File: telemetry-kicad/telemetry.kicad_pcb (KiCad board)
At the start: 4 copper layers, 94 x 83.5 mm, 97 parts, among them J1 2601-1102, J2 RFPC-SMA27-F, J3 TC2030, J4 2601-1102, J5 2601-1102, J6 USB_C_Receptacle_USB2.0_16P, J7 SD_Card_Receptacle, Q1 DMP3099LQ-7, SW1 SW_NRST, SW2 SW_BOOT0, U1 LMR33610ADDAR, U10 TLC59108IPWR, U11 MCP1703T-5002E/CB, U2 ASM330LHHXG1TR, U3 MAX-M10S-00B, U4 TCAN337, U5 STM32H523RCT7, U6 TCAN337, U7 USBLC6-2SC6, U9 TLC59108IPWR, Y1 ABM8AIG-24.000MHz-8-2Z-T

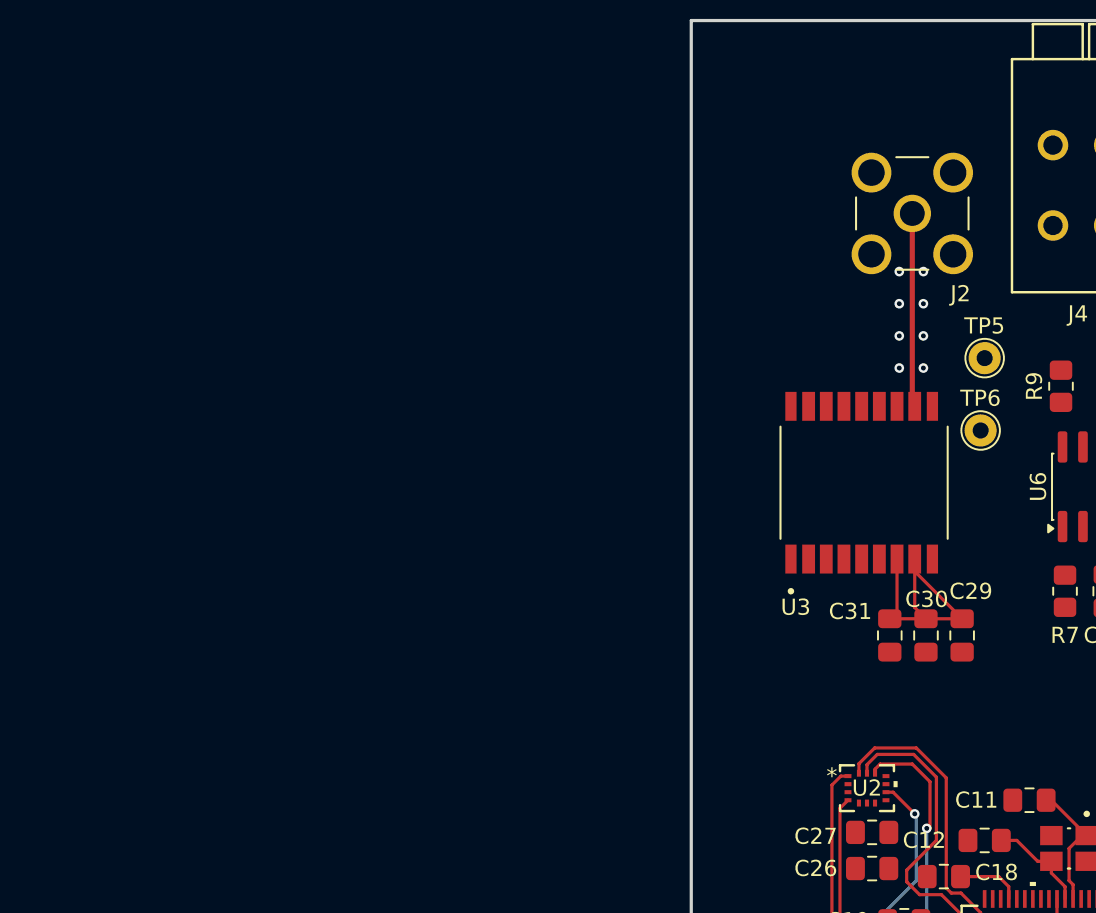
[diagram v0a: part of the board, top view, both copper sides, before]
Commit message: Changed ublox MAX-M10 to Quectel LC29HBAMD to enable the option of using RTK as well as keeping the dead reckoning features
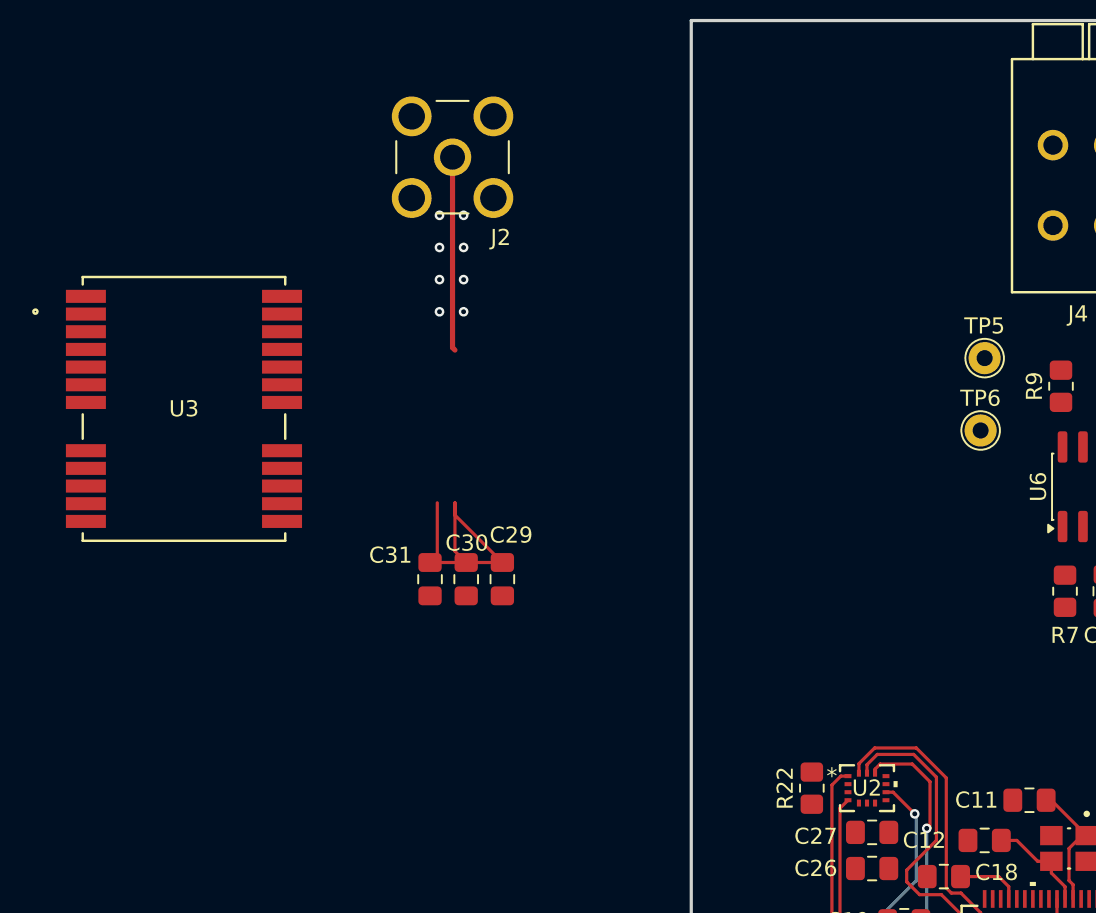
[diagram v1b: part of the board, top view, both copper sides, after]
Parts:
- added R22: 10K, Resistor_SMD:R_0805_2012Metric_Pad1.20x1.40mm_HandSolder, F.Cu at (19.5, 59.8)
- U3: value MAX-M10S-00B -> LC29HIAMD; footprint telemetry:MAX-M10S-00B -> telemetry:LC29HAAMD
- moved U3 42.4 mm to (-19.6, 36.2), turned to 0 degrees
- moved C29 28.8 mm to (0.25, 46.8)
- moved C30 28.8 mm to (-2.00, 46.8)
- moved C31 28.8 mm to (-4.25, 46.8)
- moved J2 28.8 mm to (-2.85, 20.5)
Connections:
- C32 pad 2: V_IN -> VBUS_USB
- C33 pad 2: +5V -> +3.3V
- C34 pad 2: +5V -> +3.3V
- D6 pad 1: V_IN -> VBUS_USB
- U10 pad 20: +5V -> +3.3V
- U11 pad 3: V_IN -> VBUS_USB
- U3 pad 1: GND -> unconnected-(U3-BOOT-Pad1)
- U3 pad 11: ANT -> unconnected-(U3-RF_IN-Pad11)
- U3 pad 13: unconnected-(U3-LNA_EN-Pad13) -> GND
- U3 pad 2: TXD_GNSS -> unconnected-(U3-FWD-Pad2)
- U3 pad 3: RXD_GNSS -> unconnected-(U3-1PPS-Pad3)
- U3 pad 4: TIMEPULSE_GNSS -> unconnected-(U3-WHEELTICK-Pad4)
- U3 pad 7: +3.3V -> unconnected-(U3-RESERVED-Pad7)
- U3 pad 8: +3.3V -> unconnected-(U3-RESET_N-Pad8)
- U5 pad 33: TXD_CAN2 -> RXD_CAN2
- U5 pad 34: RXD_CAN2 -> TXD_CAN2
- U9 pad 20: +5V -> +3.3V
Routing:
- net +5V: track 4.75 -> 0.00 mm
- net +3.3V: track 66.0 -> 70.7 mm

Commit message: small fixes
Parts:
- added C28: 100nF, Capacitor_SMD:C_0805_2012Metric_Pad1.18x1.45mm_HandSolder, F.Cu at (-27.7, 78.8)
- added C36: 100nF, Capacitor_SMD:C_0805_2012Metric_Pad1.18x1.45mm_HandSolder, F.Cu at (-27.7, 81.8)
- added C37: 10uF, Capacitor_SMD:C_0805_2012Metric_Pad1.18x1.45mm_HandSolder, F.Cu at (-27.7, 84.8)
- added C38: 100nF, Capacitor_SMD:C_0805_2012Metric_Pad1.18x1.45mm_HandSolder, F.Cu at (-27.7, 87.8)
- added C39: 1uF, Capacitor_SMD:C_0805_2012Metric_Pad1.18x1.45mm_HandSolder, F.Cu at (-27.7, 90.9)
- added R24: 10k, Resistor_SMD:R_0805_2012Metric_Pad1.20x1.40mm_HandSolder, F.Cu at (-14.6, 86.8)
- added R25: R_US, Resistor_THT:R_Array_SIP4, F.Cu at (-39.9, 61.6)
- added R26: R_US, Resistor_THT:R_Array_SIP4, F.Cu at (-39.9, 65.8)
- added R29: R_US, Resistor_THT:R_Array_SIP4, F.Cu at (-39.9, 69.9)
- added R30: R_US, Resistor_THT:R_Array_SIP4, F.Cu at (-39.9, 74.1)
- added R31: 21.5k, Resistor_THT:R_Array_SIP4, F.Cu at (-39.9, 78.3)
- added U13: TXS0108EPW, Package_SO:TSSOP-20_4.4x6.5mm_P0.65mm, F.Cu at (-20.6, 81.3)
- added U8: TPS2121RUXR, telemetry:VQFN-HR-12_L2.5-W2.0-P0.50-BL, F.Cu at (-15.0, 90.0)
- R27: value 1.1k -> 1.87k
- R28: value 3.74k -> 8.66k
- U3: value LC29HIAMD -> LC29HBAMD; footprint telemetry:LC29HAAMD -> telemetry:LC29HBAMD
- moved D6 100.8 mm to (-21.1, 88.1), turned to 0 degrees
- moved U3 32.3 mm to (-20.2, 68.4)
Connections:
- C2 pad 1: VBUS_USB -> V_HV
- C3 pad 1: VBUS_USB -> V_HV
- C32 pad 2: VBUS_USB -> V_HV
- D1 pad 1: VBUS_USB -> V_HV
- D6 pad 1: VBUS_USB -> +12V
- J1 pad 1: V_IN -> +12V
- J1 pad 2: V_IN -> +12V
- Q1 pad 2: VBUS_USB -> V_HV
- TP1 pad 1: VBUS_USB -> V_HV
- U1 pad 2: VBUS_USB -> V_HV
- U1 pad 3: VBUS_USB -> V_HV
- U11 pad 3: VBUS_USB -> V_HV
- U3 pad 11: unconnected-(U3-RF_IN-Pad11) -> ANT
- U3 pad 18: unconnected-(U3-CTS/SPI_MOSI-Pad18) -> CS_GNSS_1.8V
- U3 pad 19: unconnected-(U3-RTS/SPI_MISO-Pad19) -> CLK_GNSS_1.8V
- U3 pad 20: unconnected-(U3-TXD/SPI_CLK-Pad20) -> MISO_GNSS_1.8V
- U3 pad 21: unconnected-(U3-RXD/SPI_CS-Pad21) -> MOSI_GNSS_1.8V
- U3 pad 22: unconnected-(U3-RESERVED-Pad22) -> +3.3V
- U3 pad 23: unconnected-(U3-VCC-Pad23) -> +3.3V
- U3 pad 3: unconnected-(U3-1PPS-Pad3) -> TIMERIN_GNSS_1.8V
- U3 pad 5: unconnected-(U3-D_SEL-Pad5) -> Net-(U3-D_SEL1)
- U3 pad 7: unconnected-(U3-RESERVED-Pad7) -> VDD_EXT
- U3 pad 8: unconnected-(U3-RESET_N-Pad8) -> RESET_GNSS_1.8V
- U3 pad 9: unconnected-(U3-VDD_RF-Pad9) -> +3.3V
- U5 pad 10: unconnected-(U5A-PC2-Pad10) -> SW_C
- U5 pad 11: unconnected-(U5A-PC3-Pad11) -> SW_D
- U5 pad 14: unconnected-(U5A-PA0-Pad14) -> MOSI_GNSS
- U5 pad 15: unconnected-(U5A-PA1-Pad15) -> MISO_GNSS
- U5 pad 16: unconnected-(U5A-PA2-Pad16) -> CLK_GNSS
- U5 pad 17: unconnected-(U5A-PA3-Pad17) -> CS_GNSS
- U5 pad 35: RXD_GNSS -> unconnected-(U5A-PB14-Pad35)
- U5 pad 36: TXD_GNSS -> unconnected-(U5A-PB15-Pad36)
- U5 pad 37: TIMEPULSE_GNSS -> RESET_GNSS
- U5 pad 42: unconnected-(U5A-PA9-Pad42) -> TIMERIN_GNSS
- U5 pad 8: unconnected-(U5A-PC0-Pad8) -> SW_A
- U5 pad 9: unconnected-(U5A-PC1-Pad9) -> SW_B
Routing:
- net VBUS_USB: track 22.7 -> 8.06 mm, vias 1 -> 0
- net V_HV: track 0.00 -> 14.7 mm, vias 0 -> 1

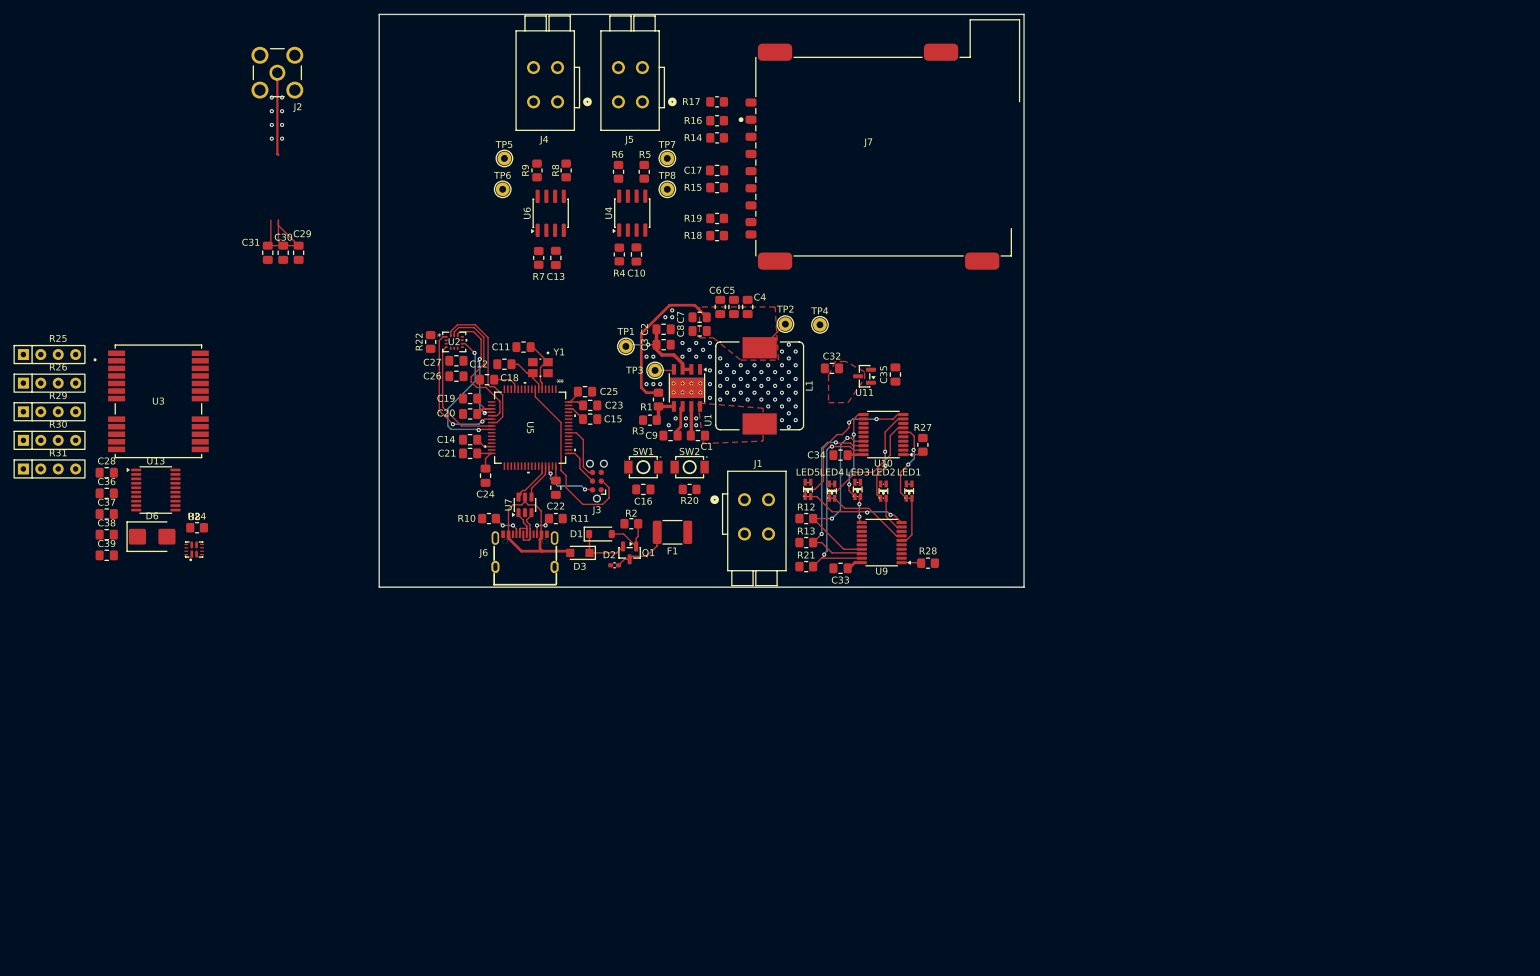
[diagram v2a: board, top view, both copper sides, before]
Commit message: All 3d files added, layout mostly done. some progress routing. schematic is finalised. Switched to microsd card.
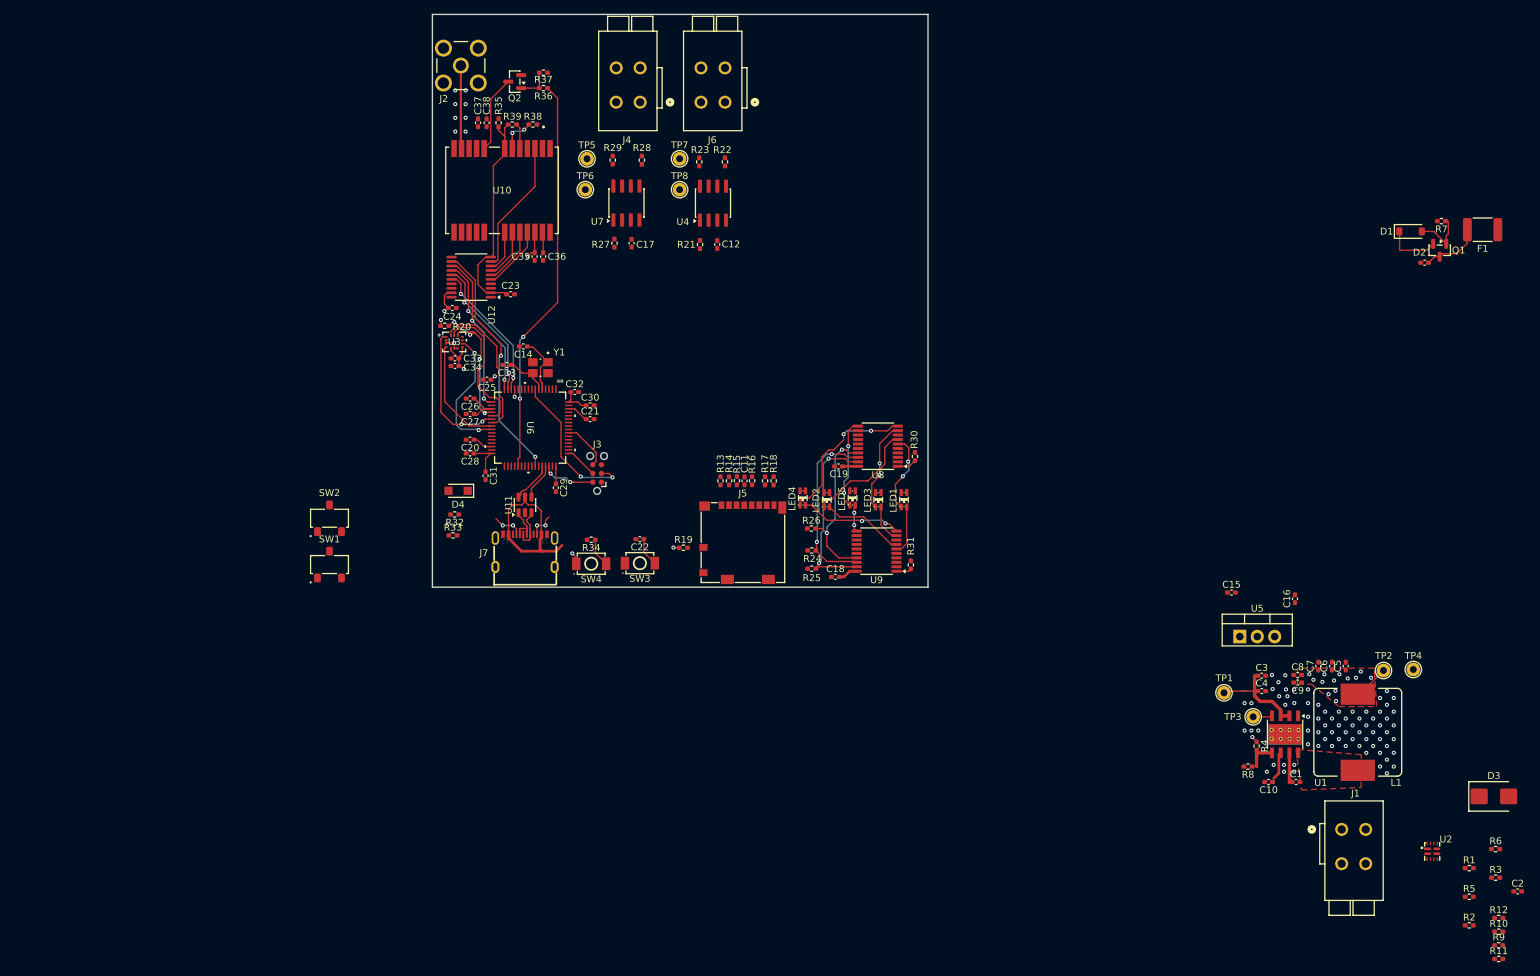
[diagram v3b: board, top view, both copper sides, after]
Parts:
- removed the C37 at (-27.7, 84.8)
- removed the J7 at (105.3, 34.2)
- removed the U11 at (82.8, 64.8)
- added J5: MOLEX_104031-0811, telemetry:MOLEX_104031-0811, F.Cu at (65.0, 89.0)
- added Q2: MMBT3904, Package_TO_SOT_SMD:SOT-23, F.Cu at (31.8, 21.8)
- added R10: 63.4k, Resistor_SMD:R_0402_1005Metric_Pad0.72x0.64mm_HandSolder, F.Cu at (175.2, 145.7)
- added R11: 5k, Resistor_SMD:R_0402_1005Metric_Pad0.72x0.64mm_HandSolder, F.Cu at (175.2, 149.7)
- added R12: 5k, Resistor_SMD:R_0402_1005Metric_Pad0.72x0.64mm_HandSolder, F.Cu at (175.2, 143.7)
- added R19: 10k, Resistor_SMD:R_0402_1005Metric_Pad0.72x0.64mm_HandSolder, F.Cu at (56.3, 89.8)
- added R36: 10k, Resistor_SMD:R_0402_1005Metric_Pad0.72x0.64mm_HandSolder, F.Cu at (35.9, 22.8)
- added R37: 100k, Resistor_SMD:R_0402_1005Metric_Pad0.72x0.64mm_HandSolder, F.Cu at (35.9, 20.5)
- added R38: 39k, Resistor_SMD:R_0402_1005Metric_Pad0.72x0.64mm_HandSolder, F.Cu at (34.4, 28.1)
- added R39: 39k, Resistor_SMD:R_0402_1005Metric_Pad0.72x0.64mm_HandSolder, F.Cu at (31.4, 28.1)
- added R9: 10.2k, Resistor_SMD:R_0402_1005Metric_Pad0.72x0.64mm_HandSolder, F.Cu at (175.2, 147.7)
- added SW1: CJS-1200TB1, telemetry:CJS-1200TB1, F.Cu at (4.75, 92.2)
- added SW2: CJS-1200TB1, telemetry:CJS-1200TB1, F.Cu at (4.75, 85.5)
- added U5: LM2940CT-5.0/LF01, telemetry:LM2940CT-5.0-LF01, F.Cu at (137.5, 102.7)
- C1, C38: footprint Capacitor_SMD:C_0805_2012Metric_Pad1.18x1.45mm_HandSolder -> Capacitor_SMD:C_0402_1005Metric_Pad0.74x0.62mm_HandSolder
- C10: renamed from C9; footprint Capacitor_SMD:C_0805_2012Metric_Pad1.18x1.45mm_HandSolder -> Capacitor_SMD:C_0402_1005Metric_Pad0.74x0.62mm_HandSolder
- C11: renamed from C17; footprint Capacitor_SMD:C_0805_2012Metric_Pad1.18x1.45mm_HandSolder -> Capacitor_SMD:C_0402_1005Metric_Pad0.74x0.62mm_HandSolder
- C12: renamed from C10; footprint Capacitor_SMD:C_0805_2012Metric_Pad1.18x1.45mm_HandSolder -> Capacitor_SMD:C_0402_1005Metric_Pad0.74x0.62mm_HandSolder
- C13: renamed from C11; footprint Capacitor_SMD:C_0805_2012Metric_Pad1.18x1.45mm_HandSolder -> Capacitor_SMD:C_0402_1005Metric_Pad0.74x0.62mm_HandSolder
- C14: renamed from C12; footprint Capacitor_SMD:C_0805_2012Metric_Pad1.18x1.45mm_HandSolder -> Capacitor_SMD:C_0402_1005Metric_Pad0.74x0.62mm_HandSolder
- C15: renamed from C32; footprint Capacitor_SMD:C_0805_2012Metric_Pad1.18x1.45mm_HandSolder -> Capacitor_SMD:C_0402_1005Metric_Pad0.74x0.62mm_HandSolder
- C16: renamed from C35; value 1uF -> 22uF; footprint Capacitor_SMD:C_0805_2012Metric_Pad1.18x1.45mm_HandSolder -> Capacitor_SMD:C_0402_1005Metric_Pad0.74x0.62mm_HandSolder
- C17: renamed from C13; footprint Capacitor_SMD:C_0805_2012Metric_Pad1.18x1.45mm_HandSolder -> Capacitor_SMD:C_0402_1005Metric_Pad0.74x0.62mm_HandSolder
- C18: renamed from C33; footprint Capacitor_SMD:C_0805_2012Metric_Pad1.18x1.45mm_HandSolder -> Capacitor_SMD:C_0402_1005Metric_Pad0.74x0.62mm_HandSolder
- C19: renamed from C34; footprint Capacitor_SMD:C_0805_2012Metric_Pad1.18x1.45mm_HandSolder -> Capacitor_SMD:C_0402_1005Metric_Pad0.74x0.62mm_HandSolder
- C2: renamed from C39; footprint Capacitor_SMD:C_0805_2012Metric_Pad1.18x1.45mm_HandSolder -> Capacitor_SMD:C_0402_1005Metric_Pad0.74x0.62mm_HandSolder
- C20: renamed from C14; footprint Capacitor_SMD:C_0805_2012Metric_Pad1.18x1.45mm_HandSolder -> Capacitor_SMD:C_0402_1005Metric_Pad0.74x0.62mm_HandSolder
- C21: renamed from C15; footprint Capacitor_SMD:C_0805_2012Metric_Pad1.18x1.45mm_HandSolder -> Capacitor_SMD:C_0402_1005Metric_Pad0.74x0.62mm_HandSolder
- C22: renamed from C16; footprint Capacitor_SMD:C_0805_2012Metric_Pad1.18x1.45mm_HandSolder -> Capacitor_SMD:C_0402_1005Metric_Pad0.74x0.62mm_HandSolder
- C23: renamed from C36; footprint Capacitor_SMD:C_0805_2012Metric_Pad1.18x1.45mm_HandSolder -> Capacitor_SMD:C_0402_1005Metric_Pad0.74x0.62mm_HandSolder
- C24: renamed from C28; footprint Capacitor_SMD:C_0805_2012Metric_Pad1.18x1.45mm_HandSolder -> Capacitor_SMD:C_0402_1005Metric_Pad0.74x0.62mm_HandSolder
- C25: renamed from C18; footprint Capacitor_SMD:C_0805_2012Metric_Pad1.18x1.45mm_HandSolder -> Capacitor_SMD:C_0402_1005Metric_Pad0.74x0.62mm_HandSolder
- C26: renamed from C19; footprint Capacitor_SMD:C_0805_2012Metric_Pad1.18x1.45mm_HandSolder -> Capacitor_SMD:C_0402_1005Metric_Pad0.74x0.62mm_HandSolder
- C27: renamed from C20; footprint Capacitor_SMD:C_0805_2012Metric_Pad1.18x1.45mm_HandSolder -> Capacitor_SMD:C_0402_1005Metric_Pad0.74x0.62mm_HandSolder
- C28: renamed from C21; footprint Capacitor_SMD:C_0805_2012Metric_Pad1.18x1.45mm_HandSolder -> Capacitor_SMD:C_0402_1005Metric_Pad0.74x0.62mm_HandSolder
- C29: renamed from C22; footprint Capacitor_SMD:C_0805_2012Metric_Pad1.18x1.45mm_HandSolder -> Capacitor_SMD:C_0402_1005Metric_Pad0.74x0.62mm_HandSolder
- C3: renamed from C2; footprint Capacitor_SMD:C_0805_2012Metric_Pad1.18x1.45mm_HandSolder -> Capacitor_SMD:C_0402_1005Metric_Pad0.74x0.62mm_HandSolder
- C30: renamed from C23; footprint Capacitor_SMD:C_0805_2012Metric_Pad1.18x1.45mm_HandSolder -> Capacitor_SMD:C_0402_1005Metric_Pad0.74x0.62mm_HandSolder
- C31: renamed from C24; footprint Capacitor_SMD:C_0805_2012Metric_Pad1.18x1.45mm_HandSolder -> Capacitor_SMD:C_0402_1005Metric_Pad0.74x0.62mm_HandSolder
- C32: renamed from C25; footprint Capacitor_SMD:C_0805_2012Metric_Pad1.18x1.45mm_HandSolder -> Capacitor_SMD:C_0402_1005Metric_Pad0.74x0.62mm_HandSolder
- C33: renamed from C26; footprint Capacitor_SMD:C_0805_2012Metric_Pad1.18x1.45mm_HandSolder -> Capacitor_SMD:C_0402_1005Metric_Pad0.74x0.62mm_HandSolder
- C34: renamed from C27; footprint Capacitor_SMD:C_0805_2012Metric_Pad1.18x1.45mm_HandSolder -> Capacitor_SMD:C_0402_1005Metric_Pad0.74x0.62mm_HandSolder
- C35: renamed from C29; footprint Capacitor_SMD:C_0805_2012Metric_Pad1.18x1.45mm_HandSolder -> Capacitor_SMD:C_0402_1005Metric_Pad0.74x0.62mm_HandSolder
- C36: renamed from C30; footprint Capacitor_SMD:C_0805_2012Metric_Pad1.18x1.45mm_HandSolder -> Capacitor_SMD:C_0402_1005Metric_Pad0.74x0.62mm_HandSolder
- C37: renamed from C31; footprint Capacitor_SMD:C_0805_2012Metric_Pad1.18x1.45mm_HandSolder -> Capacitor_SMD:C_0402_1005Metric_Pad0.74x0.62mm_HandSolder
- C4: renamed from C3; footprint Capacitor_SMD:C_0805_2012Metric_Pad1.18x1.45mm_HandSolder -> Capacitor_SMD:C_0402_1005Metric_Pad0.74x0.62mm_HandSolder
- C5: renamed from C4; footprint Capacitor_SMD:C_0805_2012Metric_Pad1.18x1.45mm_HandSolder -> Capacitor_SMD:C_0402_1005Metric_Pad0.74x0.62mm_HandSolder
- C6: renamed from C5; footprint Capacitor_SMD:C_0805_2012Metric_Pad1.18x1.45mm_HandSolder -> Capacitor_SMD:C_0402_1005Metric_Pad0.74x0.62mm_HandSolder
- C7: renamed from C6; footprint Capacitor_SMD:C_0805_2012Metric_Pad1.18x1.45mm_HandSolder -> Capacitor_SMD:C_0402_1005Metric_Pad0.74x0.62mm_HandSolder
- C8: renamed from C7; footprint Capacitor_SMD:C_0805_2012Metric_Pad1.18x1.45mm_HandSolder -> Capacitor_SMD:C_0402_1005Metric_Pad0.74x0.62mm_HandSolder
- C9: renamed from C8; footprint Capacitor_SMD:C_0805_2012Metric_Pad1.18x1.45mm_HandSolder -> Capacitor_SMD:C_0402_1005Metric_Pad0.74x0.62mm_HandSolder
- LED1: footprint telemetry:LED-SMD_4P-L2.0-W1.3-RD-TL -> telemetry:XL-2012SURUGC
- LED2: renamed from LED4; footprint telemetry:LED-SMD_4P-L2.0-W1.3-RD-TL -> telemetry:XL-2012SURUGC
- LED3: renamed from LED2; footprint telemetry:LED-SMD_4P-L2.0-W1.3-RD-TL -> telemetry:XL-2012SURUGC
- LED4: renamed from LED5; footprint telemetry:LED-SMD_4P-L2.0-W1.3-RD-TL -> telemetry:XL-2012SURUGC
- LED5: renamed from LED3; footprint telemetry:LED-SMD_4P-L2.0-W1.3-RD-TL -> telemetry:XL-2012SURUGC
- R1: renamed from R25; value R_US -> 23.7k; footprint Resistor_THT:R_Array_SIP4 -> Resistor_SMD:R_0402_1005Metric_Pad0.72x0.64mm_HandSolder
- R13: renamed from R17; footprint Resistor_SMD:R_0805_2012Metric_Pad1.20x1.40mm_HandSolder -> Resistor_SMD:R_0402_1005Metric_Pad0.72x0.64mm_HandSolder
- R14: renamed from R16; footprint Resistor_SMD:R_0805_2012Metric_Pad1.20x1.40mm_HandSolder -> Resistor_SMD:R_0402_1005Metric_Pad0.72x0.64mm_HandSolder
- R15: renamed from R14; footprint Resistor_SMD:R_0805_2012Metric_Pad1.20x1.40mm_HandSolder -> Resistor_SMD:R_0402_1005Metric_Pad0.72x0.64mm_HandSolder
- R16: renamed from R15; footprint Resistor_SMD:R_0805_2012Metric_Pad1.20x1.40mm_HandSolder -> Resistor_SMD:R_0402_1005Metric_Pad0.72x0.64mm_HandSolder
- R17: renamed from R19; footprint Resistor_SMD:R_0805_2012Metric_Pad1.20x1.40mm_HandSolder -> Resistor_SMD:R_0402_1005Metric_Pad0.72x0.64mm_HandSolder
- R18: footprint Resistor_SMD:R_0805_2012Metric_Pad1.20x1.40mm_HandSolder -> Resistor_SMD:R_0402_1005Metric_Pad0.72x0.64mm_HandSolder
- R2: renamed from R29; value R_US -> 18.2k; footprint Resistor_THT:R_Array_SIP4 -> Resistor_SMD:R_0402_1005Metric_Pad0.72x0.64mm_HandSolder
- R20: renamed from R22; footprint Resistor_SMD:R_0805_2012Metric_Pad1.20x1.40mm_HandSolder -> Resistor_SMD:R_0402_1005Metric_Pad0.72x0.64mm_HandSolder
- R21: renamed from R4; footprint Resistor_SMD:R_0805_2012Metric_Pad1.20x1.40mm_HandSolder -> Resistor_SMD:R_0402_1005Metric_Pad0.72x0.64mm_HandSolder
- R22: renamed from R5; footprint Resistor_SMD:R_0805_2012Metric_Pad1.20x1.40mm_HandSolder -> Resistor_SMD:R_0402_1005Metric_Pad0.72x0.64mm_HandSolder
- R23: renamed from R6; footprint Resistor_SMD:R_0805_2012Metric_Pad1.20x1.40mm_HandSolder -> Resistor_SMD:R_0402_1005Metric_Pad0.72x0.64mm_HandSolder
- R24: renamed from R13; footprint Resistor_SMD:R_0805_2012Metric_Pad1.20x1.40mm_HandSolder -> Resistor_SMD:R_0402_1005Metric_Pad0.72x0.64mm_HandSolder
- R25: renamed from R21; footprint Resistor_SMD:R_0805_2012Metric_Pad1.20x1.40mm_HandSolder -> Resistor_SMD:R_0402_1005Metric_Pad0.72x0.64mm_HandSolder
- R26: renamed from R12; footprint Resistor_SMD:R_0805_2012Metric_Pad1.20x1.40mm_HandSolder -> Resistor_SMD:R_0402_1005Metric_Pad0.72x0.64mm_HandSolder
- R27: renamed from R7; footprint Resistor_SMD:R_0805_2012Metric_Pad1.20x1.40mm_HandSolder -> Resistor_SMD:R_0402_1005Metric_Pad0.72x0.64mm_HandSolder
- R28: renamed from R8; footprint Resistor_SMD:R_0805_2012Metric_Pad1.20x1.40mm_HandSolder -> Resistor_SMD:R_0402_1005Metric_Pad0.72x0.64mm_HandSolder
- R29: renamed from R9; footprint Resistor_SMD:R_0805_2012Metric_Pad1.20x1.40mm_HandSolder -> Resistor_SMD:R_0402_1005Metric_Pad0.72x0.64mm_HandSolder
- R3: renamed from R31; footprint Resistor_THT:R_Array_SIP4 -> Resistor_SMD:R_0402_1005Metric_Pad0.72x0.64mm_HandSolder
- R30: renamed from R27; footprint Resistor_SMD:R_0805_2012Metric_Pad1.20x1.40mm_HandSolder -> Resistor_SMD:R_0402_1005Metric_Pad0.72x0.64mm_HandSolder
- R31: renamed from R28; value 8.66k -> 1.87k; footprint Resistor_SMD:R_0805_2012Metric_Pad1.20x1.40mm_HandSolder -> Resistor_SMD:R_0402_1005Metric_Pad0.72x0.64mm_HandSolder
- R32: renamed from R10; footprint Resistor_SMD:R_0805_2012Metric_Pad1.20x1.40mm_HandSolder -> Resistor_SMD:R_0402_1005Metric_Pad0.72x0.64mm_HandSolder
- R33: renamed from R11; footprint Resistor_SMD:R_0805_2012Metric_Pad1.20x1.40mm_HandSolder -> Resistor_SMD:R_0402_1005Metric_Pad0.72x0.64mm_HandSolder
- R34: renamed from R20; footprint Resistor_SMD:R_0805_2012Metric_Pad1.20x1.40mm_HandSolder -> Resistor_SMD:R_0402_1005Metric_Pad0.72x0.64mm_HandSolder
- R35: renamed from R24; footprint Resistor_SMD:R_0805_2012Metric_Pad1.20x1.40mm_HandSolder -> Resistor_SMD:R_0402_1005Metric_Pad0.72x0.64mm_HandSolder
- R4: renamed from R1; footprint Resistor_SMD:R_0805_2012Metric_Pad1.20x1.40mm_HandSolder -> Resistor_SMD:R_0402_1005Metric_Pad0.72x0.64mm_HandSolder
- R5: renamed from R26; value R_US -> 5k; footprint Resistor_THT:R_Array_SIP4 -> Resistor_SMD:R_0402_1005Metric_Pad0.72x0.64mm_HandSolder
- R6: renamed from R30; value R_US -> 5k; footprint Resistor_THT:R_Array_SIP4 -> Resistor_SMD:R_0402_1005Metric_Pad0.72x0.64mm_HandSolder
- R7: renamed from R2; footprint Resistor_SMD:R_0805_2012Metric_Pad1.20x1.40mm_HandSolder -> Resistor_SMD:R_0402_1005Metric_Pad0.72x0.64mm_HandSolder
- R8: renamed from R3; footprint Resistor_SMD:R_0805_2012Metric_Pad1.20x1.40mm_HandSolder -> Resistor_SMD:R_0402_1005Metric_Pad0.72x0.64mm_HandSolder
- moved R1 223.7 mm to (170.9, 136.5)
- moved R2 223.7 mm to (170.9, 144.8)
- moved R5 223.7 mm to (170.9, 140.6)
- moved R3 222.7 mm to (174.8, 137.8)
- moved R6 222.7 mm to (174.8, 133.7)
- moved C2 211.4 mm to (178.0, 139.8)
- moved D3 199.2 mm to (174.5, 126.0)
- moved U2 185.8 mm to (165.5, 134.0), turned to -90 degrees
- moved D1 126.1 mm to (162.3, 43.6)
- moved F1 126.1 mm to (172.8, 43.4)
- moved Q1 126.1 mm to (166.6, 46.4)
- moved R7 126.1 mm to (166.8, 42.1)
- moved D2 126.1 mm to (164.4, 48.2)
- moved C5 101.7 mm to (152.9, 107.0)
- moved C6 101.7 mm to (150.9, 107.0)
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- renumbered D6 to D3, D3 to D4, J5 to J6, J6 to J7, SW1 to SW3, SW2 to SW4, U3 to U10, U7 to U11, U13 to U12, U8 to U2, U2 to U3, U5 to U6, U6 to U7, U10 to U8
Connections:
- C15 pad 2: V_HV -> V_IN
- C3 pad 1: V_HV -> V_IN
- C4 pad 1: V_HV -> V_IN
- D1 pad 1: V_HV -> +12V
- D3 pad 1: +12V -> +12V_IN
- F1 pad 1: V_IN -> +12V_IN
- J1 pad 1: +12V -> +12V_IN
- J1 pad 2: +12V -> +12V_IN
- Q1 pad 2: V_HV -> +12V
- R1 pad 2: DIV2_MUX -> OV2_MUX
- R2 pad 2: DIV1_MUX -> PR1_MUX
- R5 pad 1: DIV2_MUX -> OV2_MUX
- R6 pad 1: DIV1_MUX -> PR1_MUX
- TP1 pad 1: V_HV -> V_IN
- U1 pad 2: V_HV -> V_IN
- U1 pad 3: V_HV -> V_IN
- U10 pad 18: CS_GNSS_1.8V -> CS_GNSS_2V8
- U10 pad 19: CLK_GNSS_1.8V -> CLK_GNSS_2V8
- U10 pad 20: MISO_GNSS_1.8V -> MISO_GNSS_2V8
- U10 pad 21: MOSI_GNSS_1.8V -> MOSI_GNSS_2V8
- U10 pad 3: TIMERIN_GNSS_1.8V -> TIMERIN_GNSS_2V8
- U10 pad 5: Net-(U3-D_SEL1) -> DSEL_1
- U10 pad 6: unconnected-(U3-D_SEL2-Pad6) -> DSEL_2
- U10 pad 8: RESET_GNSS_1.8V -> GNSS_RESET_N
- U12 pad 1: MOSI_GNSS_1.8V -> unconnected-(U12-A1-Pad1)
- U12 pad 12: unconnected-(U13-B8-Pad12) -> TIMERIN_GNSS
- U12 pad 13: unconnected-(U13-B7-Pad13) -> CS_GNSS
- U12 pad 14: RESET_GNSS -> CLK_GNSS
- U12 pad 15: TIMERIN_GNSS -> MISO_GNSS
- U12 pad 16: CS_GNSS -> MOSI_GNSS
- U12 pad 17: CLK_GNSS -> unconnected-(U12-B3-Pad17)
- U12 pad 18: MISO_GNSS -> unconnected-(U12-B2-Pad18)
- U12 pad 20: MOSI_GNSS -> unconnected-(U12-B1-Pad20)
- U12 pad 3: MISO_GNSS_1.8V -> unconnected-(U12-A2-Pad3)
- U12 pad 4: CLK_GNSS_1.8V -> unconnected-(U12-A3-Pad4)
- U12 pad 5: CS_GNSS_1.8V -> MOSI_GNSS_2V8
- U12 pad 6: TIMERIN_GNSS_1.8V -> MISO_GNSS_2V8
- U12 pad 7: RESET_GNSS_1.8V -> CLK_GNSS_2V8
- U12 pad 8: unconnected-(U13-A7-Pad8) -> CS_GNSS_2V8
- U12 pad 9: unconnected-(U13-A8-Pad9) -> TIMERIN_GNSS_2V8
- U2 pad 3: DIV2_MUX -> CP2_MUX
- U2 pad 4: DIV2_MUX -> OV2_MUX
- U2 pad 5: DIV1_MUX -> OV1_MUX
- U2 pad 6: DIV1_MUX -> PR1_MUX
- U6 pad 37: RESET_GNSS -> GNSS_RESET_ASSERT
- U6 pad 50: PG_BUCK -> unconnected-(U6A-PA15-Pad50)
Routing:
- net GNSS_RESET_ASSERT: track 0.00 -> 58.1 mm, vias 0 -> 2
- net TIMERIN_GNSS: track 0.00 -> 35.5 mm, vias 0 -> 2
- net VDD_EXT: track 0.00 -> 32.1 mm
- net CS_GNSS: track 0.00 -> 23.1 mm, vias 0 -> 2
- net CLK_GNSS: track 0.00 -> 21.1 mm, vias 0 -> 2
- net MISO_GNSS: track 0.00 -> 21.0 mm, vias 0 -> 2
- net +3.3V: track 70.7 -> 49.8 mm, vias 3 -> 22
- net MOSI_GNSS: track 0.00 -> 20.4 mm, vias 0 -> 2
- net TIMERIN_GNSS_2V8: track 0.00 -> 19.6 mm
- net V_IN: track 0.00 -> 15.2 mm
- net V_HV: track 14.7 -> 0.00 mm, vias 1 -> 0
- net GNSS_RESET_N: track 0.00 -> 11.2 mm
- net MOSI_GNSS_2V8: track 0.00 -> 9.47 mm
- net MISO_GNSS_2V8: track 0.00 -> 8.41 mm
- net +12V: track 0.00 -> 8.06 mm
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- removed copper zone on F.Cu, net V_IN
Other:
- board size 94 x 83.5 mm -> 72.2 x 83.5 mm
